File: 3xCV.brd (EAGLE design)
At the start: 98.1 x 50.2 mm, 85 parts, among them IC1 TL074, IC2 TL074, IC3 TL074, SW1 TL2285, SW2 TL2285

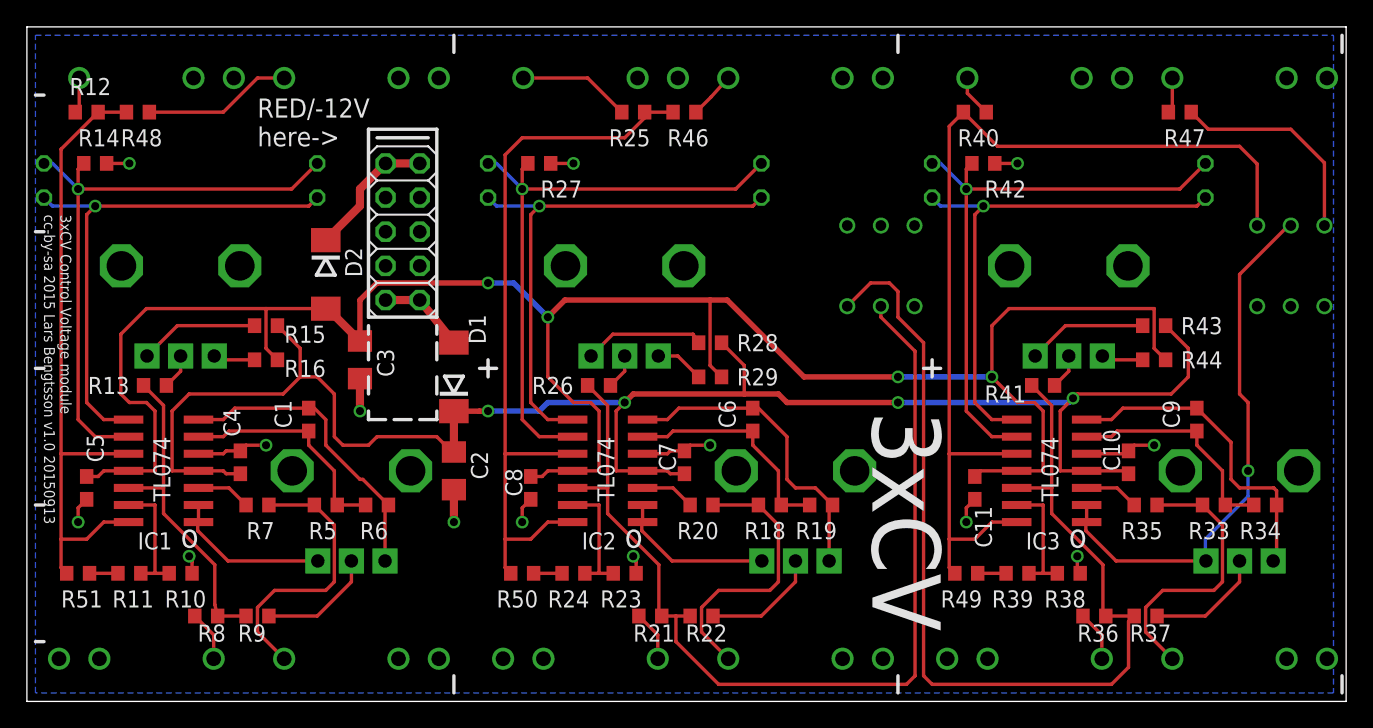
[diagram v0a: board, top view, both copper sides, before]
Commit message: Minor routing adjustments/optimized traces
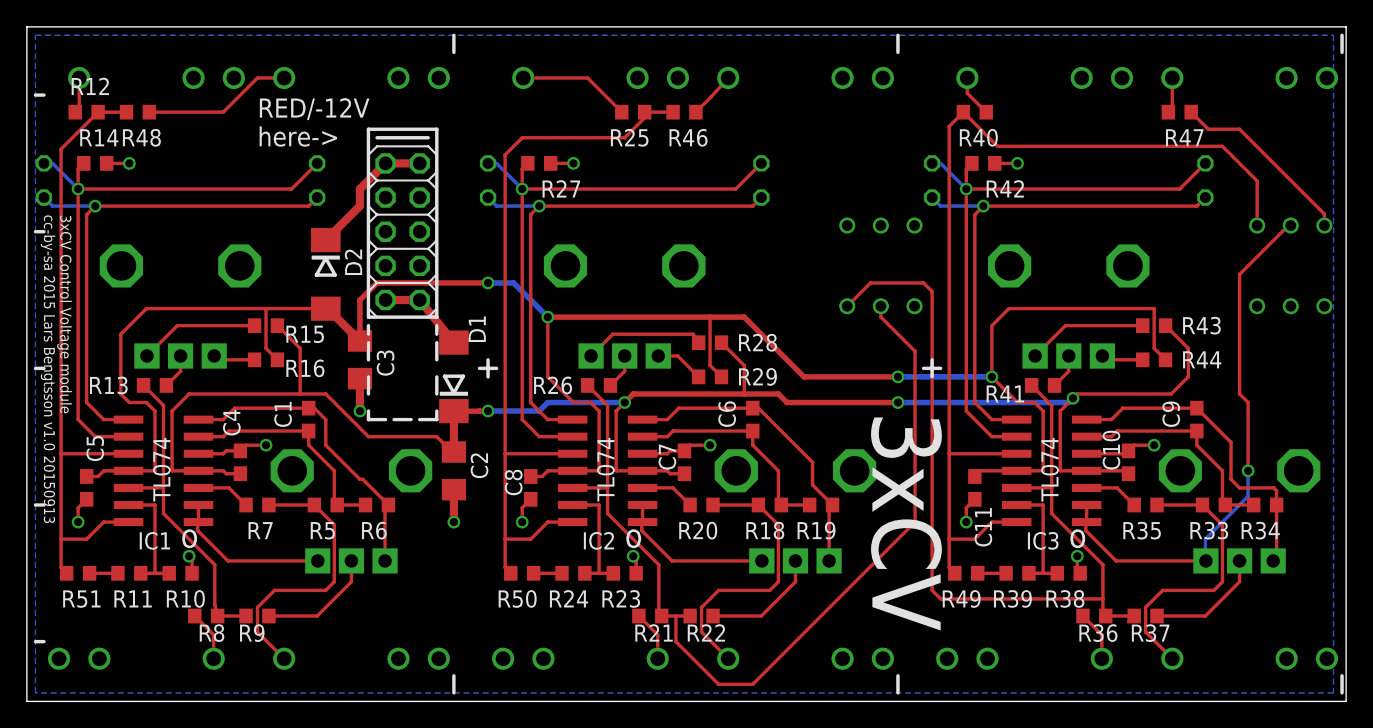
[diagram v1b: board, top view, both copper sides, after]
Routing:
- net MIX1: track 79.0 -> 67.9 mm
- net MIX2: track 73.9 -> 67.2 mm
- net -12V: track 155.6 -> 153.3 mm
- net N$18: track 16.1 -> 13.9 mm
- net +12V: track 131.2 -> 129.1 mm
- net N$26: track 23.6 -> 22.7 mm
- net N$47: track 73.5 -> 72.7 mm
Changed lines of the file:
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@@
 <wire x1="12.065" y1="22.86" x2="12.065" y2="27.305" width="0.254" layer="1"/>
 <wire x1="12.065" y1="27.305" x2="13.335" y2="28.575" width="0.254" layer="1"/>
-<wire x1="13.335" y1="28.575" x2="20.32" y2="28.575" width="0.254" layer="1"/>
-<wire x1="20.32" y1="28.575" x2="21.59" y2="29.845" width="0.254" layer="1"/>
-<wire x1="21.59" y1="29.845" x2="22.86" y2="29.845" width="0.254" layer="1"/>
-<wire x1="22.86" y1="29.845" x2="24.13" y2="28.575" width="0.254" layer="1"/>
-<wire x1="24.13" y1="28.575" x2="24.13" y2="25.4" width="0.254" layer="1"/>
-<wire x1="24.13" y1="25.4" x2="24.765" y2="24.765" width="0.254" layer="1"/>
-<wire x1="24.765" y1="24.765" x2="26.67" y2="24.765" width="0.254" layer="1"/>
-<wire x1="26.67" y1="24.765" x2="27.305" y2="25.4" width="0.254" layer="1"/>
-<wire x1="27.305" y1="25.4" x2="31.75" y2="25.4" width="0.254" layer="1"/>
+<wire x1="13.335" y1="28.575" x2="21.59" y2="28.575" width="0.254" layer="1"/>
+<wire x1="21.59" y1="28.575" x2="23.495" y2="28.575" width="0.254" layer="1"/>
+<wire x1="23.495" y1="28.575" x2="26.67" y2="25.4" width="0.254" layer="1"/>
+<wire x1="26.67" y1="25.4" x2="31.75" y2="25.4" width="0.254" layer="1"/>
 <wire x1="31.75" y1="25.4" x2="32.385" y2="24.765" width="0.254" layer="1"/>
 <wire x1="32.385" y1="24.765" x2="33.02" y2="24.765" width="0.254" layer="1"/>
@@
 <wire x1="87.63" y1="29.845" x2="87.63" y2="31.965" width="0.254" layer="1"/>
 <wire x1="87.63" y1="31.965" x2="85.94" y2="33.655" width="0.254" layer="1"/>
-<wire x1="21.59" y1="29.845" x2="21.59" y2="31.965" width="0.254" layer="1"/>
+<wire x1="21.59" y1="28.575" x2="21.59" y2="31.965" width="0.254" layer="1"/>
 <wire x1="21.59" y1="31.965" x2="19.9" y2="33.655" width="0.254" layer="1"/>
 <wire x1="54.61" y1="30.695" x2="52.92" y2="32.385" width="0.254" layer="1"/>
@@
 <wire x1="41.91" y1="27.94" x2="40.005" y2="29.845" width="0.254" layer="1"/>
 <wire x1="40.005" y1="29.845" x2="40.005" y2="34.29" width="0.254" layer="1"/>
-<wire x1="52.07" y1="35.56" x2="52.07" y2="30.695" width="0.254" layer="1"/>
+<wire x1="52.07" y1="34.29" x2="52.07" y2="30.695" width="0.254" layer="1"/>
 <wire x1="52.07" y1="30.695" x2="52.92" y2="29.845" width="0.254" layer="1"/>
 <wire x1="74.87" y1="22.86" x2="72.175" y2="22.86" width="0.254" layer="1"/>
@@
 <wire x1="37.465" y1="36.83" x2="40.005" y2="34.29" width="0.4064" layer="16"/>
 <via x="40.005" y="34.29" extent="1-16" drill="0.6" shape="octagon"/>
-<wire x1="40.005" y1="34.29" x2="41.275" y2="35.56" width="0.4064" layer="1"/>
-<wire x1="41.275" y1="35.56" x2="52.07" y2="35.56" width="0.4064" layer="1"/>
-<wire x1="52.07" y1="35.56" x2="53.34" y2="35.56" width="0.4064" layer="1"/>
-<wire x1="53.34" y1="35.56" x2="59.055" y2="29.845" width="0.4064" layer="1"/>
+<wire x1="40.005" y1="34.29" x2="52.07" y2="34.29" width="0.4064" layer="1"/>
+<wire x1="52.07" y1="34.29" x2="54.61" y2="34.29" width="0.4064" layer="1"/>
+<wire x1="54.61" y1="34.29" x2="59.055" y2="29.845" width="0.4064" layer="1"/>
 <wire x1="59.055" y1="29.845" x2="66.04" y2="29.845" width="0.4064" layer="1"/>
 <via x="66.04" y="29.845" extent="1-16" drill="0.6" shape="octagon"/>
@@
 <wire x1="60.92" y1="20.065" x2="61.175" y2="20.32" width="0.254" layer="1"/>
 <wire x1="55.245" y1="27.52" x2="55.665" y2="27.52" width="0.254" layer="1"/>
-<wire x1="55.665" y1="27.52" x2="57.785" y2="25.4" width="0.254" layer="1"/>
-<wire x1="57.785" y1="25.4" x2="57.785" y2="22.225" width="0.254" layer="1"/>
-<wire x1="57.785" y1="22.225" x2="58.42" y2="21.59" width="0.254" layer="1"/>
-<wire x1="58.42" y1="21.59" x2="59.905" y2="21.59" width="0.254" layer="1"/>
-<wire x1="59.905" y1="21.59" x2="61.175" y2="20.32" width="0.254" layer="1"/>
+<wire x1="55.665" y1="27.52" x2="59.69" y2="23.495" width="0.254" layer="1"/>
+<wire x1="59.69" y1="23.495" x2="59.69" y2="21.805" width="0.254" layer="1"/>
+<wire x1="59.69" y1="21.805" x2="61.175" y2="20.32" width="0.254" layer="1"/>
 </signal>
 <signal name="N$27">
@@
 <contactref element="SW1" pad="2"/>
 <wire x1="49.53" y1="12.065" x2="48.475" y2="12.065" width="0.254" layer="1"/>
-<wire x1="67.31" y1="31.75" x2="67.31" y2="7.62" width="0.254" layer="1"/>
-<wire x1="67.31" y1="7.62" x2="66.675" y2="6.985" width="0.254" layer="1"/>
-<wire x1="66.675" y1="6.985" x2="52.705" y2="6.985" width="0.254" layer="1"/>
+<wire x1="67.31" y1="31.75" x2="67.31" y2="19.05" width="0.254" layer="1"/>
+<wire x1="67.31" y1="19.05" x2="55.245" y2="6.985" width="0.254" layer="1"/>
+<wire x1="55.245" y1="6.985" x2="52.705" y2="6.985" width="0.254" layer="1"/>
 <wire x1="52.705" y1="6.985" x2="49.53" y2="10.16" width="0.254" layer="1"/>
 <wire x1="49.53" y1="10.16" x2="49.53" y2="12.065" width="0.254" layer="1"/>
@@
 <wire x1="77.47" y1="21.59" x2="77.47" y2="19.685" width="0.254" layer="1"/>
 <wire x1="77.47" y1="19.685" x2="81.28" y2="15.875" width="0.254" layer="1"/>
-<wire x1="81.28" y1="15.875" x2="81.28" y2="12.28" width="0.254" layer="1"/>
+<wire x1="81.28" y1="15.875" x2="81.28" y2="13.335" width="0.254" layer="1"/>
+<wire x1="81.28" y1="13.335" x2="81.28" y2="12.28" width="0.254" layer="1"/>
 <wire x1="81.28" y1="12.28" x2="81.495" y2="12.065" width="0.254" layer="1"/>
 <wire x1="81.495" y1="12.065" x2="83.605" y2="12.065" width="0.254" layer="1"/>
@@
 <wire x1="77.47" y1="27.725" x2="75.985" y2="29.21" width="0.254" layer="1"/>
 <contactref element="SW1" pad="3"/>
-<wire x1="67.945" y1="32.385" x2="67.945" y2="7.62" width="0.254" layer="1"/>
-<wire x1="67.945" y1="7.62" x2="68.58" y2="6.985" width="0.254" layer="1"/>
-<wire x1="68.58" y1="6.985" x2="81.915" y2="6.985" width="0.254" layer="1"/>
-<wire x1="81.915" y1="6.985" x2="83.185" y2="8.255" width="0.254" layer="1"/>
-<wire x1="83.185" y1="8.255" x2="83.185" y2="11.645" width="0.254" layer="1"/>
+<wire x1="68.58" y1="36.195" x2="68.58" y2="13.97" width="0.254" layer="1"/>
 <wire x1="83.185" y1="11.645" x2="83.605" y2="12.065" width="0.254" layer="1"/>
-<wire x1="67.945" y1="32.385" x2="66.04" y2="34.29" width="0.254" layer="1"/>
-<wire x1="66.04" y1="34.29" x2="66.04" y2="36.195" width="0.254" layer="1"/>
-<wire x1="66.04" y1="36.195" x2="65.405" y2="36.83" width="0.254" layer="1"/>
-<wire x1="65.405" y1="36.83" x2="64" y2="36.83" width="0.254" layer="1"/>
+<wire x1="68.58" y1="36.195" x2="67.945" y2="36.83" width="0.254" layer="1"/>
+<wire x1="67.945" y1="36.83" x2="64" y2="36.83" width="0.254" layer="1"/>
 <wire x1="64" y1="36.83" x2="62.27" y2="35.1" width="0.254" layer="1"/>
+<wire x1="68.58" y1="13.97" x2="69.215" y2="13.335" width="0.254" layer="1"/>
+<wire x1="69.215" y1="13.335" x2="81.28" y2="13.335" width="0.254" layer="1"/>
 </signal>
 <signal name="N$47">
@@
 <contactref element="SW2" pad="6"/>
 <wire x1="69.85" y1="48.475" x2="70.905" y2="49.53" width="0.254" layer="1"/>
-<wire x1="92.75" y1="41.1" x2="92.75" y2="45.68" width="0.254" layer="1"/>
-<wire x1="92.75" y1="45.68" x2="91.44" y2="46.99" width="0.254" layer="1"/>
-<wire x1="91.44" y1="46.99" x2="73.445" y2="46.99" width="0.254" layer="1"/>
+<wire x1="92.75" y1="41.1" x2="92.75" y2="44.41" width="0.254" layer="1"/>
+<wire x1="92.75" y1="44.41" x2="90.17" y2="46.99" width="0.254" layer="1"/>
+<wire x1="90.17" y1="46.99" x2="73.445" y2="46.99" width="0.254" layer="1"/>
 <wire x1="73.445" y1="46.99" x2="70.905" y2="49.53" width="0.254" layer="1"/>
 </signal>
@@
 <contactref element="SW2" pad="4"/>
 <contactref element="R47" pad="1"/>
-<wire x1="97.75" y1="41.1" x2="97.75" y2="45.76" width="0.254" layer="1"/>
-<wire x1="97.75" y1="45.76" x2="95.25" y2="48.26" width="0.254" layer="1"/>
-<wire x1="95.25" y1="48.26" x2="89.115" y2="48.26" width="0.254" layer="1"/>
+<wire x1="97.75" y1="41.1" x2="97.75" y2="41.95" width="0.254" layer="1"/>
+<wire x1="97.75" y1="41.95" x2="91.44" y2="48.26" width="0.254" layer="1"/>
+<wire x1="91.44" y1="48.26" x2="89.115" y2="48.26" width="0.254" layer="1"/>
 <wire x1="89.115" y1="48.26" x2="87.845" y2="49.53" width="0.254" layer="1"/>
 </signal>

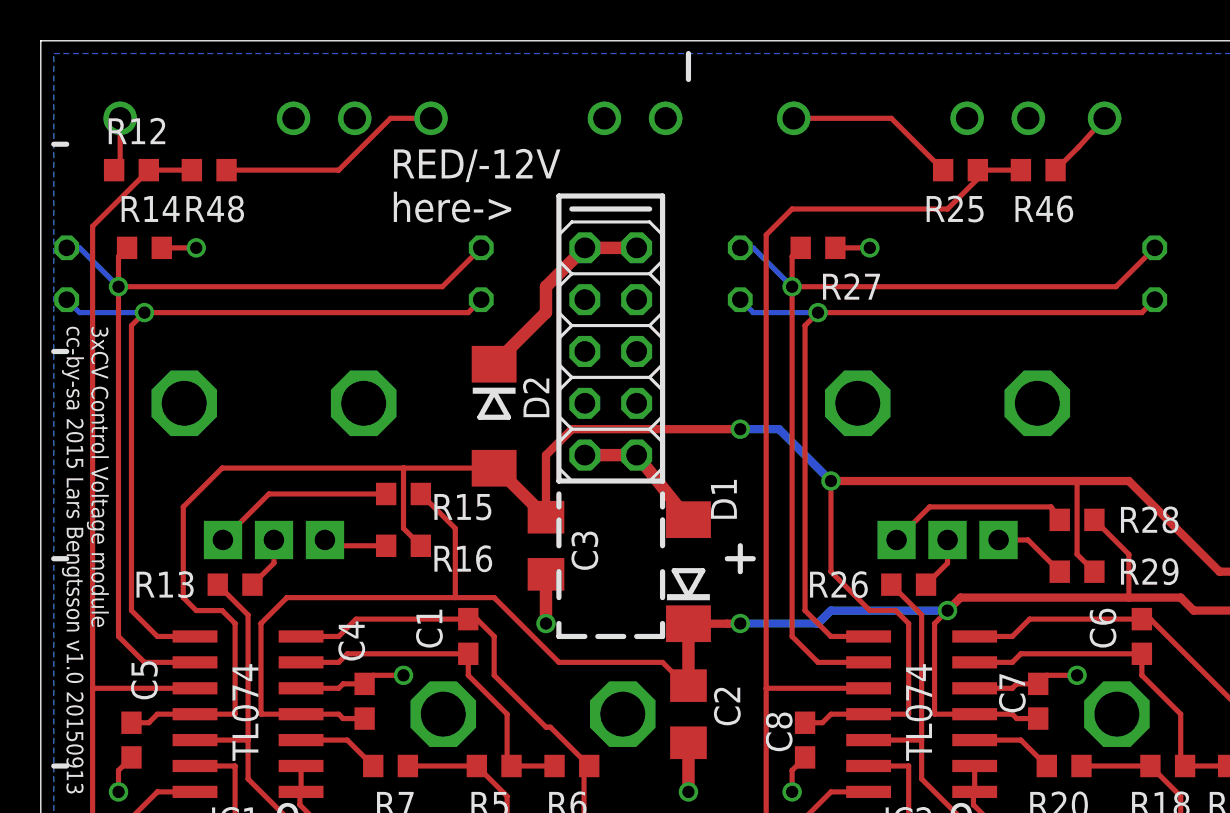
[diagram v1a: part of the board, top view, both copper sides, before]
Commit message: Moved resistors around output of unit 2, moved a few other labels.
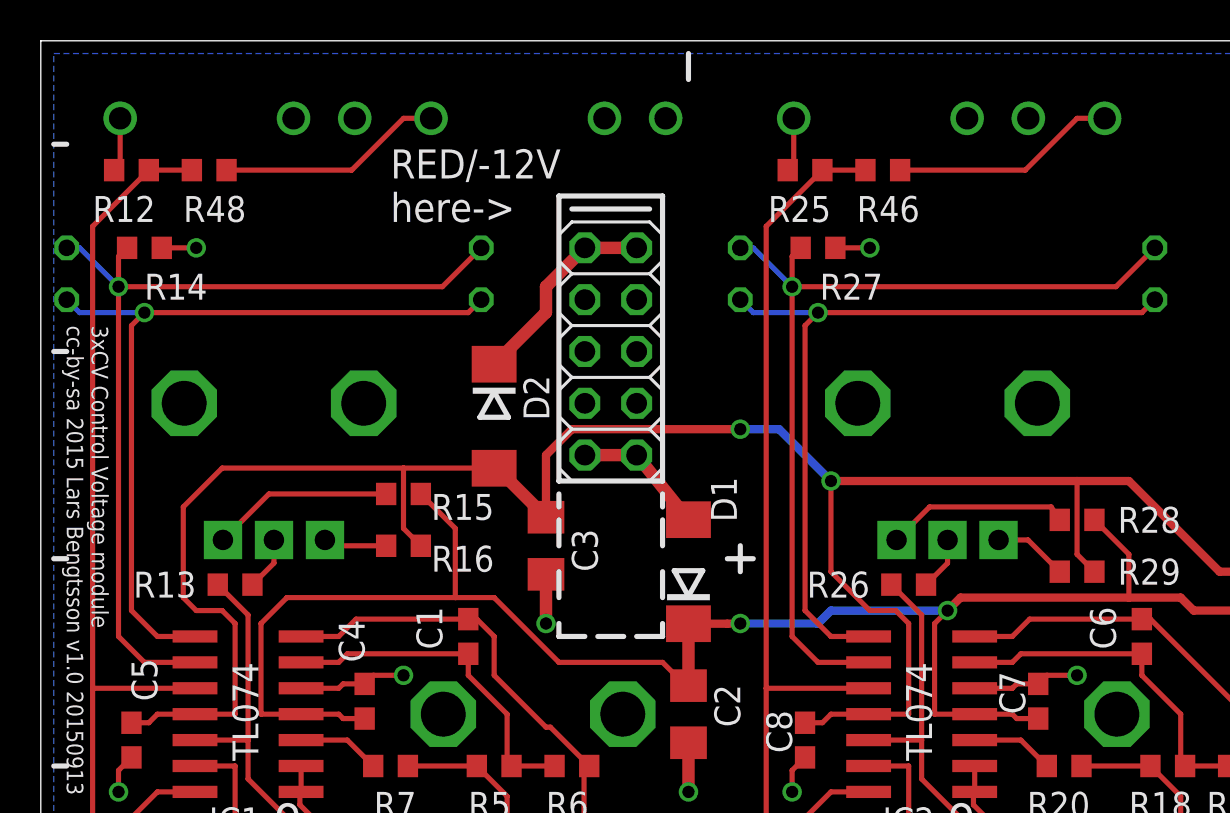
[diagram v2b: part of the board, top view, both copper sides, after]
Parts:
- moved R25 7.62 mm to (38.7, 49.5)
- moved R46 7.62 mm to (42.5, 49.5)
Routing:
- net N$57: track 55.9 -> 48.3 mm
- net N$19: track 3.50 -> 11.1 mm
- net N$32: track 8.38 -> 2.66 mm
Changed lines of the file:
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@@
 </element>
 <element name="R12" library="rcl" package="R0603" value="220" x="5.715" y="49.53" smashed="yes" rot="R180">
-<attribute name="NAME" x="4.445" y="50.8" size="1.27" layer="25"/>
+<attribute name="NAME" x="3.81" y="46.99" size="1.27" layer="25"/>
 <attribute name="VALUE" x="6.35" y="51.435" size="1.27" layer="27" rot="R180"/>
 </element>
@@
 </element>
 <element name="R14" library="rcl" package="R0603" value="1k" x="6.35" y="45.72" smashed="yes" rot="R180">
-<attribute name="NAME" x="5.08" y="46.99" size="1.27" layer="25"/>
+<attribute name="NAME" x="6.35" y="43.18" size="1.27" layer="25"/>
 <attribute name="VALUE" x="6.985" y="47.625" size="1.27" layer="27" rot="R180"/>
 </element>
@@
 <attribute name="VALUE" x="41.275" y="13.335" size="1.27" layer="27"/>
 </element>
-<element name="R25" library="rcl" package="R0603" value="220" x="46.355" y="49.53" smashed="yes" rot="R180">
-<attribute name="NAME" x="47.625" y="48.26" size="1.27" layer="25" rot="R180"/>
-<attribute name="VALUE" x="46.99" y="51.435" size="1.27" layer="27" rot="R180"/>
+<element name="R25" library="rcl" package="R0603" value="220" x="38.735" y="49.53" smashed="yes" rot="R180">
+<attribute name="NAME" x="40.005" y="48.26" size="1.27" layer="25" rot="R180"/>
+<attribute name="VALUE" x="39.37" y="51.435" size="1.27" layer="27" rot="R180"/>
 </element>
 <element name="R26" library="rcl" package="R0603" value="100k" x="43.815" y="29.21" smashed="yes" rot="R180">
@@
 </element>
 <element name="OUT3" library="thonkiconn" package="WQP-PJ301M-12_JACK" value="WQP-PJ301M-12_JACK" x="58.42" y="52.07" rot="MR270"/>
-<element name="R46" library="rcl" package="R0603" value="220" x="50.165" y="49.53" smashed="yes">
-<attribute name="NAME" x="48.895" y="46.99" size="1.27" layer="25"/>
-<attribute name="VALUE" x="49.53" y="47.625" size="1.27" layer="27"/>
+<element name="R46" library="rcl" package="R0603" value="220" x="42.545" y="49.53" smashed="yes">
+<attribute name="NAME" x="41.275" y="46.99" size="1.27" layer="25"/>
+<attribute name="VALUE" x="41.91" y="47.625" size="1.27" layer="27"/>
 </element>
 <element name="OUT4" library="thonkiconn" package="WQP-PJ301M-12_JACK" value="WQP-PJ301M-12_JACK" x="91.44" y="52.07" rot="MR270"/>
@@
 <contactref element="OUT1" pad="P$1"/>
 <contactref element="R25" pad="2"/>
-<wire x1="38.18" y1="52.07" x2="42.965" y2="52.07" width="0.254" layer="1"/>
-<wire x1="42.965" y1="52.07" x2="45.505" y2="49.53" width="0.254" layer="1"/>
+<wire x1="38.18" y1="52.07" x2="38.18" y2="49.825" width="0.254" layer="1"/>
+<wire x1="38.18" y1="49.825" x2="37.885" y2="49.53" width="0.254" layer="1"/>
 </signal>
 <signal name="N$33">
@@
 <contactref element="R46" pad="2"/>
 <contactref element="OUT3" pad="P$1"/>
-<wire x1="53.42" y1="52.07" x2="52.15" y2="50.665" width="0.254" layer="1"/>
-<wire x1="52.15" y1="50.665" x2="51.015" y2="49.53" width="0.254" layer="1"/>
+<wire x1="53.42" y1="52.07" x2="52.07" y2="52.07" width="0.254" layer="1"/>
+<wire x1="52.07" y1="52.07" x2="49.53" y2="49.53" width="0.254" layer="1"/>
+<wire x1="49.53" y1="49.53" x2="43.395" y2="49.53" width="0.254" layer="1"/>
 </signal>
 <signal name="N$21">
@@
 <contactref element="R48" pad="2"/>
 <contactref element="OUT5" pad="P$1"/>
-<wire x1="20.4" y1="52.07" x2="18.415" y2="52.07" width="0.254" layer="1"/>
-<wire x1="18.415" y1="52.07" x2="15.875" y2="49.53" width="0.254" layer="1"/>
-<wire x1="15.875" y1="49.53" x2="10.375" y2="49.53" width="0.254" layer="1"/>
+<wire x1="20.4" y1="52.07" x2="19.05" y2="52.07" width="0.254" layer="1"/>
+<wire x1="19.05" y1="52.07" x2="16.51" y2="49.53" width="0.254" layer="1"/>
+<wire x1="16.51" y1="49.53" x2="10.375" y2="49.53" width="0.254" layer="1"/>
 </signal>
 <signal name="N$57">
@@
 <wire x1="41.85" y1="24.13" x2="36.83" y2="24.13" width="0.254" layer="1"/>
 <wire x1="36.83" y1="24.13" x2="36.83" y2="17.78" width="0.254" layer="1"/>
-<wire x1="49.315" y1="49.53" x2="47.205" y2="49.53" width="0.254" layer="1"/>
-<wire x1="36.83" y1="24.13" x2="36.83" y2="46.355" width="0.254" layer="1"/>
-<wire x1="38.1" y1="47.625" x2="45.72" y2="47.625" width="0.254" layer="1"/>
-<wire x1="45.72" y1="47.625" x2="47.205" y2="49.11" width="0.254" layer="1"/>
-<wire x1="47.205" y1="49.11" x2="47.205" y2="49.53" width="0.254" layer="1"/>
-<wire x1="36.83" y1="46.355" x2="38.1" y2="47.625" width="0.254" layer="1"/>
+<wire x1="36.83" y1="24.13" x2="36.83" y2="46.775" width="0.254" layer="1"/>
+<wire x1="39.585" y1="49.53" x2="41.695" y2="49.53" width="0.254" layer="1"/>
+<wire x1="36.83" y1="46.775" x2="39.585" y2="49.53" width="0.254" layer="1"/>
 </signal>
 <signal name="N$58">
